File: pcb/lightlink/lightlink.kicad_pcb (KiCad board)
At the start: 2 copper layers, 80 x 66 mm, 59 parts, among them J1 PIC Programming Header, J2 Wire Antenna, J3 Conn_WallSocket, J4 Conn_01x01_Socket, J5 Conn_01x01_Socket, K1 Relay_SPST-NO, Q1 Q_NMOS_DGS, SW1 SW_DIP_x04, SW2 SW_MEC_5G_2LED, U1 PIC16F18126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

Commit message: Adding Official RevA0 of the PCB design
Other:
- board text added: "5A fuse"
- board text added: "LIVE_OUT"
- board text added: "LightLink Scott Stack 2024"
- board text added: "Rev A0"
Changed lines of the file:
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@@
       (drillshape 0)
       (scaleselection 1)
-      (outputdirectory "C:/Users/Scott/Dropbox/my documents/Projects_and_Misc_Tech/1_PROJECTS/RF_OutletRemote/RemoteOutlet/Gerbers/")
+      (outputdirectory "Gerbers/")
     )
   )
@@
     (property "ki_keywords" "connector")
     (attr through_hole)
-    (fp_text reference "J5" (at -0.1 -1.3 180 unlocked) (layer "F.SilkS")
+    (fp_text reference "J5" (at 3.34 -3.1 180 unlocked) (layer "F.SilkS")
         (effects (font (size 1 1) (thickness 0.15)))
     )
@@
     (fp_line (start 1 0.625) (end 1 -0.625)
       (stroke (width 0.1) (type solid)) (layer "B.Fab"))
-    (pad "1" smd roundrect (at -1.0375 0 270) (size 1.175 1.45) (layers "B.Cu" "B.Paste" "B.Mask") (roundrect_rratio 0.212766)
+    (pad "1" smd roundrect (at -1.0375 0 270) (size 1.175 1.45) (layers "B.Cu" "B.Paste" "B.Mask") (roundrect_rratio 0.2127659574)
       (net 1 "GND") (pintype "passive"))
-    (pad "2" smd roundrect (at 1.0375 0 270) (size 1.175 1.45) (layers "B.Cu" "B.Paste" "B.Mask") (roundrect_rratio 0.212766)
+    (pad "2" smd roundrect (at 1.0375 0 270) (size 1.175 1.45) (layers "B.Cu" "B.Paste" "B.Mask") (roundrect_rratio 0.2127659574)
       (net 5 "+3.3V") (pintype "passive"))
     (model "${KICAD6_3DMODEL_DIR}/Capacitor_SMD.3dshapes/C_0805_2012Metric.wrl"
@@
   (gr_rect (start 120.84 111.4) (end 150.84 141.4)
     (stroke (width 0.15) (type default)) (fill none) (layer "User.1"))
+  (gr_text "5A fuse" (at 132.5 83.2) (layer "F.SilkS")
+    (effects (font (size 1 1) (thickness 0.15)) (justify left bottom))
+  )
+  (gr_text "Rev A0" (at 152.8 135.6) (layer "F.SilkS")
+    (effects (font (size 1 1) (thickness 0.2) bold) (justify left bottom))
+  )
+  (gr_text "LIVE_OUT" (at 122.6 118.1) (layer "F.SilkS")
+    (effects (font (size 1 1) (thickness 0.15)) (justify left bottom))
+  )
+  (gr_text "LightLink\nScott Stack 2024\n" (at 118.3 74.2) (layer "F.SilkS")
+    (effects (font (size 1 1) (thickness 0.2) bold) (justify left bottom))
+  )
   (segment (start 147.242651 87.9) (end 142.542651 92.6) (width 1.5) (layer "F.Cu") (net 1))
   (segment (start 149.8775 115.4) (end 149.8775 109.8375) (width 0.5) (layer "F.Cu") (net 1))

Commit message: Fix channel select and remove debug LED flash
Also update PCB with a few fixes from assembly and test
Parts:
- removed R15: 31.6k, Capacitor_SMD:C_0805_2012Metric_Pad1.18x1.45mm_HandSolder
- added R2: 31.6k, Capacitor_SMD:C_0805_2012Metric_Pad1.18x1.45mm_HandSolder, B.Cu at (127.6, 98.0)
- moved R14 3.62 mm to (124.1, 97.3), turned to 90 degrees
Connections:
- R14 pad 1: +3.3V -> /power/3v3_FB
- R14 pad 2: /power/3v3_FB -> GND

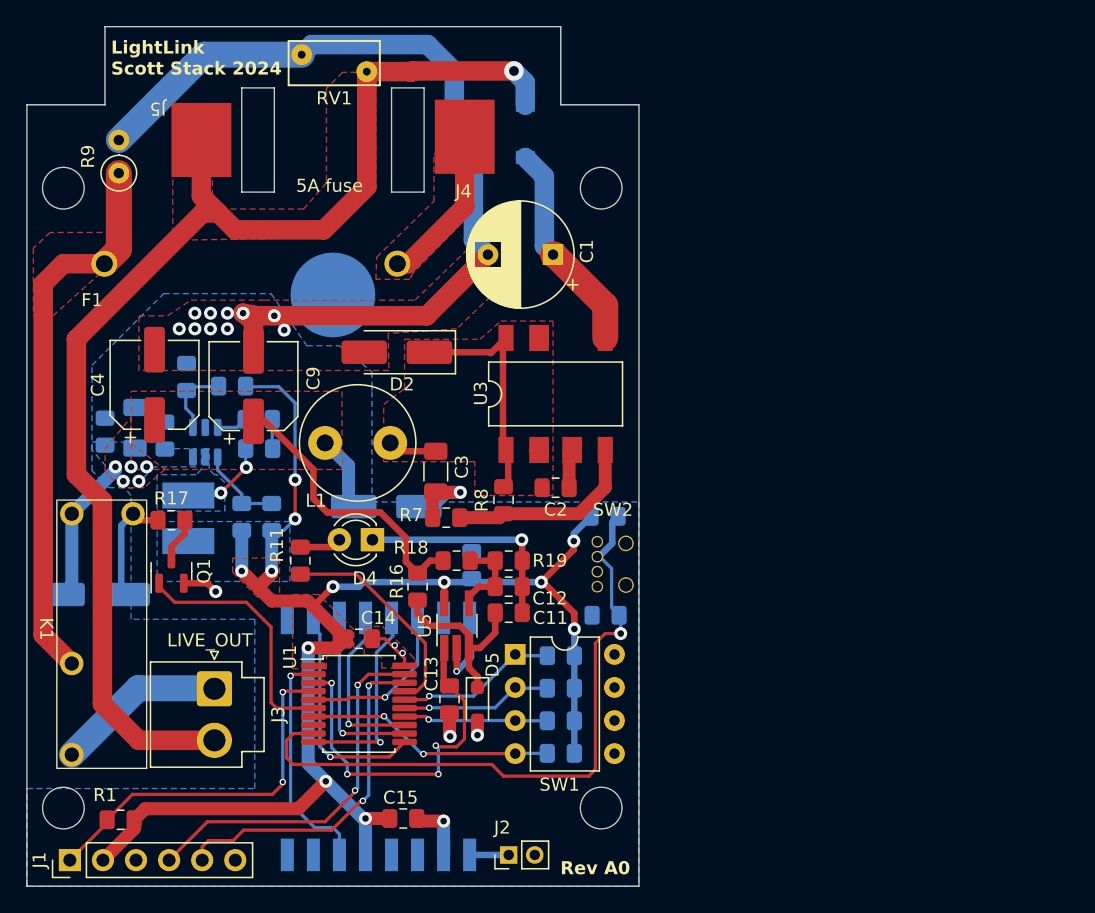
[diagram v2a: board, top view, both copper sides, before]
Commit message: Update PCB with several fixes
* Increase value of inrush limiting resistor
* Update locations of button/DIP switch
* Fix footprint for DIP switch
* Fix footprint for full bridge rectifier
* Change 1206 cap footprints to 0805
* Rotate main JST connector so that it doesn't impact the plug
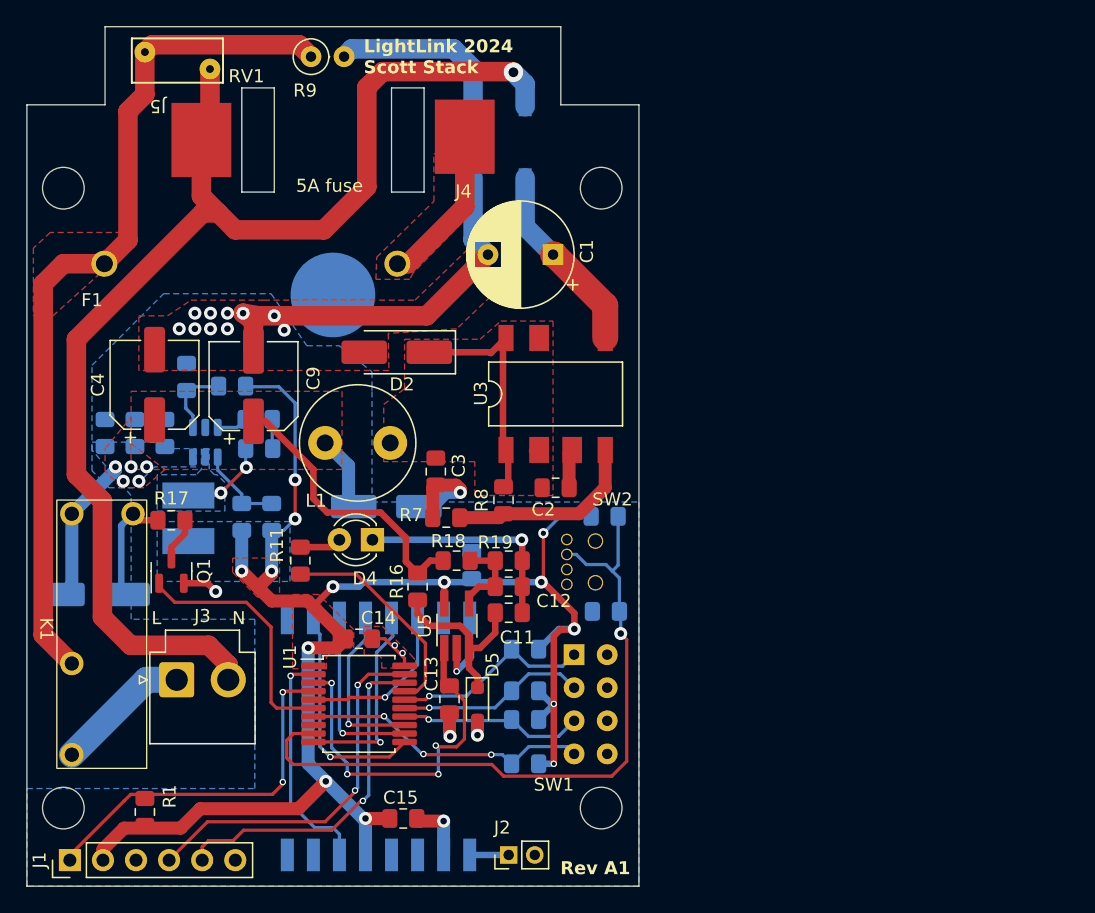
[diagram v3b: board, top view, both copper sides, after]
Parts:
- C3, C5: footprint Capacitor_SMD:C_1206_3216Metric_Pad1.33x1.80mm_HandSolder -> Capacitor_SMD:C_0805_2012Metric_Pad1.18x1.45mm_HandSolder
- R9: value 10 - Fusible -> 20
- SW1: footprint Package_DIP:DIP-8_W7.62mm -> switches_sps:DIP-8_SW_Horiz_Werth
- moved R9 17.3 mm to (133.7, 72.7), turned to 0 degrees
- moved RV1 12.0 mm to (120.9, 72.3)
- moved SW1 7.06 mm to (156.4, 118.6)
- moved J3 2.98 mm to (123.3, 120.5), turned to 0 degrees
- moved R3 2.85 mm to (150.1, 127.0)
- moved R6 2.79 mm to (150.1, 118.2)
- moved R5 2.75 mm to (150.1, 121.4)
- moved R4 2.74 mm to (150.1, 123.6)
- moved SW2 2.35 mm to (153.3, 111.5)
- moved R1 1.95 mm to (120.9, 130.7), turned to 90 degrees
- moved D1 1.14 mm to (148.1, 79.0), turned to -90 degrees
- moved C5 0.40 mm to (120.1, 101.6)
- moved C16 0.30 mm to (156.3, 115.3)
- moved C6 0.20 mm to (122.4, 101.6)
- moved R10 0.10 mm to (117.8, 101.6)
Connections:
- RV1 pad 1: /power/live_fbr_in -> LIVE_IN_FUSED
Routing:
- net LIVE_IN_FUSED: track 42.8 -> 66.3 mm
- net /power/live_fbr_in: track 32.3 -> 13.7 mm
- net +3.3V: track 118.2 -> 129.5 mm, vias 12 -> 14
- net /microcontroller_logic/BUTTON_IN: track 50.7 -> 54.4 mm
- net /microcontroller_logic/CHAN_SEL2: track 11.1 -> 14.5 mm
- net /microcontroller_logic/CHAN_SEL1: track 11.6 -> 15.0 mm
- net /microcontroller_logic/CHAN_SEL0: track 12.4 -> 15.7 mm
- net /microcontroller_logic/CHAN_SEL3: track 19.2 -> 22.4 mm, vias 2 -> 3
- net /power/12V_SW: track 22.2 -> 19.1 mm
- net LIVE_OUT: track 13.1 -> 10.4 mm
- net GND: track 76.8 -> 74.7 mm
- net /power/LNK_IN: track 16.5 -> 14.9 mm
- net NEUTRAL_IN: track 96.2 -> 97.0 mm
- removed copper zone on F.Cu, net NEUTRAL_IN
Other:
- board text added: "L"
- board text added: "LightLink 2024 Scott Stack"
- board text added: "N"
- board text added: "Rev A1"
- board text removed: "LIVE_OUT"
- board text removed: "LightLink Scott Stack 2024"
- board text removed: "Rev A0"
